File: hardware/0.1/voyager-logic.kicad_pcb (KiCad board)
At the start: 6 copper layers, 0 parts

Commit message: finalise BOM
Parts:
- added C201: 4u7, Capacitor_SMD:C_0402_1005Metric, F.Cu at (120.8, 54.4)
- added C202: 10u, Capacitor_SMD:C_0603_1608Metric, F.Cu at (110.0, 65.5)
- added C203: 470n, Capacitor_SMD:C_0402_1005Metric, F.Cu at (118.0, 56.9)
- added C204: 100n, Capacitor_SMD:C_0402_1005Metric, F.Cu at (116.6, 58.9)
- added C205: 470n, Capacitor_SMD:C_0402_1005Metric, F.Cu at (122.3, 52.4)
- added C206: 470n, Capacitor_SMD:C_0402_1005Metric, F.Cu at (112.6, 52.6)
- added C207: 470n, Capacitor_SMD:C_0402_1005Metric, F.Cu at (124.0, 50.4)
- added C208: 100n, Capacitor_SMD:C_0402_1005Metric, F.Cu at (118.0, 55.0)
- added C301: 100n, Capacitor_SMD:C_0402_1005Metric, F.Cu at (145.7, 64.8)
- added C302: 100n, Capacitor_SMD:C_0402_1005Metric, F.Cu at (150.2, 60.8)
- added C303: 13p, Capacitor_SMD:C_0402_1005Metric, F.Cu at (154.2, 56.3)
- added C304: 13p, Capacitor_SMD:C_0402_1005Metric, F.Cu at (157.1, 54.3)
- added C305: 100n, Capacitor_SMD:C_0402_1005Metric, F.Cu at (157.1, 52.3)
- added C306: 100n, Capacitor_SMD:C_0402_1005Metric, F.Cu at (148.6, 62.8)
- added C401: 100n, Capacitor_SMD:C_0402_1005Metric, F.Cu at (130.6, 54.3)
- added C501: 100n, Capacitor_SMD:C_0402_1005Metric, F.Cu at (178.3, 100.6)
- added C502: 100n, Capacitor_SMD:C_0402_1005Metric, F.Cu at (187.2, 91.7)
- added C701: 10u, Capacitor_SMD:C_0603_1608Metric, F.Cu at (121.8, 130.7)
- added C702: 10u, Capacitor_SMD:C_0603_1608Metric, F.Cu at (125.8, 132.7)
- added C703: 6p8, Capacitor_SMD:C_0402_1005Metric, F.Cu at (131.1, 144.2)
- added C704: 4u7, Capacitor_SMD:C_0402_1005Metric, F.Cu at (145.0, 129.1)
- added C705: 10u, Capacitor_SMD:C_0603_1608Metric, F.Cu at (121.8, 133.2)
- added C706: 100n, Capacitor_SMD:C_0402_1005Metric, F.Cu at (130.6, 140.2)
- added C707: 100n, Capacitor_SMD:C_0402_1005Metric, F.Cu at (135.2, 135.4)
- added C708: 100n, Capacitor_SMD:C_0402_1005Metric, F.Cu at (146.6, 127.1)
- added C709: 100n, Capacitor_SMD:C_0402_1005Metric, F.Cu at (145.0, 131.1)
- added C710: 100n, Capacitor_SMD:C_0402_1005Metric, F.Cu at (139.2, 129.1)
- added C711: 100n, Capacitor_SMD:C_0402_1005Metric, F.Cu at (133.5, 137.4)
- added C712: 10u, Capacitor_SMD:C_0603_1608Metric, F.Cu at (117.2, 141.2)
- added C713: 100n, Capacitor_SMD:C_0402_1005Metric, F.Cu at (136.4, 139.3)
- added C714: 100n, Capacitor_SMD:C_0402_1005Metric, F.Cu at (136.4, 137.4)
- added C715: 100n, Capacitor_SMD:C_0402_1005Metric, F.Cu at (131.1, 142.2)
- added C716: 100n, Capacitor_SMD:C_0402_1005Metric, F.Cu at (142.1, 129.1)
- added C717: 100n, Capacitor_SMD:C_0402_1005Metric, F.Cu at (138.1, 135.0)
- added C718: 4u7, Capacitor_SMD:C_0402_1005Metric, F.Cu at (127.7, 140.2)
- added C719: 100n, Capacitor_SMD:C_0402_1005Metric, F.Cu at (128.3, 142.2)
- added C720: 100n, Capacitor_SMD:C_0402_1005Metric, F.Cu at (140.9, 133.1)
- added C721: 10u, Capacitor_SMD:C_0603_1608Metric, F.Cu at (130.7, 127.4)
- added C722: 10u, Capacitor_SMD:C_0603_1608Metric, F.Cu at (121.3, 138.2)
- added C723: 6p8, Capacitor_SMD:C_0402_1005Metric, F.Cu at (130.7, 138.2)
- added C724: 4u7, Capacitor_SMD:C_0402_1005Metric, F.Cu at (125.4, 143.2)
- added C725: 10u, Capacitor_SMD:C_0603_1608Metric, F.Cu at (117.2, 138.7)
- added C726: 10u, Capacitor_SMD:C_0603_1608Metric, F.Cu at (125.8, 130.1)
- added C727: 100n, Capacitor_SMD:C_0402_1005Metric, F.Cu at (143.7, 127.1)
- added C728: 100n, Capacitor_SMD:C_0402_1005Metric, F.Cu at (142.1, 131.1)
- added C729: 100n, Capacitor_SMD:C_0402_1005Metric, F.Cu at (133.5, 139.4)
- added C730: 10u, Capacitor_SMD:C_0603_1608Metric, F.Cu at (129.8, 129.9)
- added C731: 10u, Capacitor_SMD:C_0603_1608Metric, F.Cu at (121.8, 135.7)
- added C732: 100n, Capacitor_SMD:C_0402_1005Metric, F.Cu at (138.1, 133.1)
- added C733: 100n, Capacitor_SMD:C_0402_1005Metric, F.Cu at (139.2, 131.1)
- added C734: 10u, Capacitor_SMD:C_0603_1608Metric, F.Cu at (126.7, 127.4)
- added C735: 10u, Capacitor_SMD:C_0603_1608Metric, F.Cu at (117.2, 136.2)
- added C736: 6p8, Capacitor_SMD:C_0402_1005Metric, F.Cu at (135.2, 133.4)
- added C737: 4u7, Capacitor_SMD:C_0402_1005Metric, F.Cu at (128.3, 144.2)
- added D201: SMF9.0CA, josh-passives-smt:D_SOD-123FL, F.Cu at (110.1, 62.8)
- added D202: DESD5V0U1BL, josh-passives-smt:D_X1-DFN1006-2, F.Cu at (114.4, 62.8)
- added D203: DESD5V0U1BL, josh-passives-smt:D_X1-DFN1006-2, F.Cu at (111.5, 55.4)
- added D401: LED_RGBA, josh-led:LED_TRI_2020, F.Cu at (110.3, 107.4)
- added D402: LED_RGBA, josh-led:LED_TRI_2020, F.Cu at (110.3, 79.6)
- added D501: DESD5V0U1BL, josh-passives-smt:D_X1-DFN1006-2, F.Cu at (166.4, 88.2)
- added D502: DESD5V0U1BL, josh-passives-smt:D_X1-DFN1006-2, F.Cu at (164.7, 101.5)
- added D503: DESD5V0U1BL, josh-passives-smt:D_X1-DFN1006-2, F.Cu at (174.9, 91.2)
- added D504: DESD5V0U1BL, josh-passives-smt:D_X1-DFN1006-2, F.Cu at (166.4, 97.1)
- added D505: DESD5V0U1BL, josh-passives-smt:D_X1-DFN1006-2, F.Cu at (166.4, 94.2)
- added D506: DESD5V0U1BL, josh-passives-smt:D_X1-DFN1006-2, F.Cu at (179.2, 88.2)
- added D507: DESD5V0U1BL, josh-passives-smt:D_X1-DFN1006-2, F.Cu at (174.9, 88.2)
- added D508: DESD5V0U1BL, josh-passives-smt:D_X1-DFN1006-2, F.Cu at (170.7, 94.2)
- added D509: DESD5V0U1BL, josh-passives-smt:D_X1-DFN1006-2, F.Cu at (170.7, 91.2)
- added D510: DESD5V0U1BL, josh-passives-smt:D_X1-DFN1006-2, F.Cu at (168.9, 100.0)
- added D511: DESD5V0U1BL, josh-passives-smt:D_X1-DFN1006-2, F.Cu at (160.4, 101.5)
- added D512: DESD5V0U1BL, josh-passives-smt:D_X1-DFN1006-2, F.Cu at (170.7, 88.2)
- added D513: DESD5V0U1BL, josh-passives-smt:D_X1-DFN1006-2, F.Cu at (174.9, 94.2)
- added D514: DESD5V0U1BL, josh-passives-smt:D_X1-DFN1006-2, F.Cu at (179.2, 91.2)
- added D515: DESD5V0U1BL, josh-passives-smt:D_X1-DFN1006-2, F.Cu at (170.7, 97.1)
- added D516: DESD5V0U1BL, josh-passives-smt:D_X1-DFN1006-2, F.Cu at (166.4, 91.2)
- added F201: 500mA, josh-passives-smt:Fuse_0603_1608Metric, F.Cu at (115.9, 52.7)
- added FB201: 220R, Resistor_SMD:R_0402_1005Metric, F.Cu at (121.1, 50.4)
- added FB202: 220R, Resistor_SMD:R_0402_1005Metric, F.Cu at (113.7, 59.9)
- added FB701: 220R, Resistor_SMD:R_0402_1005Metric, F.Cu at (122.5, 143.7)
- added FB702: 220R, Resistor_SMD:R_0402_1005Metric, F.Cu at (140.8, 127.1)
- added FB703: 220R, Resistor_SMD:R_0402_1005Metric, F.Cu at (136.3, 130.4)
- added FB704: 220R, Resistor_SMD:R_0402_1005Metric, F.Cu at (127.8, 138.3)
- added H201: M2, MountingHole:MountingHole_2.2mm_M2_ISO7380_Pad, F.Cu at (110.0, 71.5)
- added H202: M2, MountingHole:MountingHole_2.2mm_M2_ISO7380_Pad, F.Cu at (155.0, 71.5)
- added H203: M2, MountingHole:MountingHole_2.2mm_M2_ISO7380_Pad, F.Cu at (110.0, 116.5)
- added H204: M2, MountingHole:MountingHole_2.2mm_M2_ISO7380_Pad, F.Cu at (155.0, 116.5)
- added J201: USB_C_Receptacle, josh-connectors:USB_C_Receptacle_Amphenol_10137062-00021LF, F.Cu at (110.3, 94.0)
- added J401: JTAG, Connector:Tag-Connect_TC2030-IDC-NL_2x03_P1.27mm_Vertical, F.Cu at (178.3, 58.6)
- added J402: JTAG, Connector:Tag-Connect_TC2030-IDC-NL_2x03_P1.27mm_Vertical, F.Cu at (167.3, 60.2)
- added J501: Probe, josh-connectors:PinSocket_2x16_P1.27mm_Horizontal, F.Cu at (151.4, 103.5)
- added L701: 2u2, Inductor_SMD:L_0805_2012Metric, F.Cu at (117.5, 133.6)
- added L702: 2u2, Inductor_SMD:L_0805_2012Metric, F.Cu at (117.5, 130.8)
- added L703: 2u2, Inductor_SMD:L_0805_2012Metric, F.Cu at (122.4, 127.5)
- added R201: 909K, Resistor_SMD:R_0402_1005Metric, F.Cu at (113.7, 57.9)
- added R202: 10K, Resistor_SMD:R_0402_1005Metric, F.Cu at (116.5, 65.4)
- added R203: 200K, Resistor_SMD:R_0402_1005Metric, F.Cu at (121.1, 48.4)
- added R204: 200K, Resistor_SMD:R_0402_1005Metric, F.Cu at (109.7, 52.6)
- added R205: 200K, Resistor_SMD:R_0402_1005Metric, F.Cu at (119.4, 52.5)
- added R206: 0R, Resistor_SMD:R_0402_1005Metric, F.Cu at (115.1, 55.0)
- added R207: 0R, Resistor_SMD:R_0402_1005Metric, F.Cu at (124.0, 48.4)
- added R301: 10K, Resistor_SMD:R_0402_1005Metric, F.Cu at (138.5, 65.4)
- added R302: 200R, Resistor_SMD:R_0402_1005Metric, F.Cu at (145.7, 62.8)
- added R303: 6K04, Resistor_SMD:R_0402_1005Metric, F.Cu at (141.4, 65.4)
- added R304: 2K2, Resistor_SMD:R_0402_1005Metric, F.Cu at (154.2, 54.3)
- added R305: 2K2, Resistor_SMD:R_0402_1005Metric, F.Cu at (150.2, 58.8)
- added R306: 10K, Resistor_SMD:R_0402_1005Metric, F.Cu at (135.6, 65.4)
- added R307: DNP, Resistor_SMD:R_0402_1005Metric, F.Cu at (154.2, 52.3)
- added R308: 10K, Resistor_SMD:R_0402_1005Metric, F.Cu at (132.7, 65.4)
- added R401: 1K, Resistor_SMD:R_0402_1005Metric, F.Cu at (127.7, 57.6)
- added R402: 10K, Resistor_SMD:R_0402_1005Metric, F.Cu at (132.7, 52.3)
- added R403: 1K, Resistor_SMD:R_0402_1005Metric, F.Cu at (127.7, 55.6)
- added R404: 1K, Resistor_SMD:R_0402_1005Metric, F.Cu at (129.8, 52.3)
- added R405: 1K, Resistor_SMD:R_0402_1005Metric, F.Cu at (124.8, 55.6)
- added R406: 1K, Resistor_SMD:R_0402_1005Metric, F.Cu at (120.9, 58.9)
- added R407: 1K, Resistor_SMD:R_0402_1005Metric, F.Cu at (124.8, 57.6)
- added R408: DNP, Resistor_SMD:R_0402_1005Metric, F.Cu at (140.4, 135.3)
- added R409: 0R0, Resistor_SMD:R_0402_1005Metric, F.Cu at (143.3, 135.3)
- added R501: 0R, Resistor_SMD:R_0402_1005Metric, F.Cu at (178.5, 93.7)
- added R502: 0R, Resistor_SMD:R_0402_1005Metric, F.Cu at (175.4, 100.6)
- added R503: 909K, Resistor_SMD:R_0402_1005Metric, F.Cu at (184.3, 93.7)
- added R504: 909K, Resistor_SMD:R_0402_1005Metric, F.Cu at (172.5, 99.6)
- added R505: 909K, Resistor_SMD:R_0402_1005Metric, F.Cu at (188.6, 89.8)
- added R506: 909K, Resistor_SMD:R_0402_1005Metric, F.Cu at (168.2, 102.5)
- added R507: 909K, Resistor_SMD:R_0402_1005Metric, F.Cu at (188.6, 87.8)
- added R508: 909K, Resistor_SMD:R_0402_1005Metric, F.Cu at (185.7, 87.8)
- added R509: 909K, Resistor_SMD:R_0402_1005Metric, F.Cu at (182.8, 87.8)
- added R510: 909K, Resistor_SMD:R_0402_1005Metric, F.Cu at (174.3, 96.6)
- added R511: 0R, Resistor_SMD:R_0402_1005Metric, F.Cu at (177.2, 96.6)
- added R512: 909K, Resistor_SMD:R_0402_1005Metric, F.Cu at (174.1, 102.6)
- added R513: 909K, Resistor_SMD:R_0402_1005Metric, F.Cu at (178.3, 98.6)
- added R514: 909K, Resistor_SMD:R_0402_1005Metric, F.Cu at (171.1, 102.5)
- added R515: 909K, Resistor_SMD:R_0402_1005Metric, F.Cu at (184.3, 91.8)
- added R516: 0R, Resistor_SMD:R_0402_1005Metric, F.Cu at (182.8, 89.8)
- added R517: 909K, Resistor_SMD:R_0402_1005Metric, F.Cu at (180.1, 95.7)
- added R518: 909K, Resistor_SMD:R_0402_1005Metric, F.Cu at (175.4, 98.6)
- added R519: 909K, Resistor_SMD:R_0402_1005Metric, F.Cu at (181.4, 93.7)
- added R520: 909K, Resistor_SMD:R_0402_1005Metric, F.Cu at (185.7, 89.8)
- added R701: 120K, Resistor_SMD:R_0402_1005Metric, F.Cu at (124.5, 141.2)
- added R702: 26K7, Resistor_SMD:R_0402_1005Metric, F.Cu at (119.6, 143.7)
- added R703: 120K, Resistor_SMD:R_0402_1005Metric, F.Cu at (132.3, 133.4)
- added R704: 120K, Resistor_SMD:R_0402_1005Metric, F.Cu at (132.1, 135.4)
- added R705: 120K, Resistor_SMD:R_0402_1005Metric, F.Cu at (137.9, 127.1)
- added R706: 60K4, Resistor_SMD:R_0402_1005Metric, F.Cu at (116.7, 143.5)
- added SW401: KMR2, josh-buttons-switches:SW_Push_KMR2, F.Cu at (140.6, 57.1)
- added TP201: TP, josh-test-point:TestPoint_SMDPad_D0.5mm_NO_SILK, F.Cu at (118.0, 62.8)
- added TP202: TP, josh-test-point:TestPoint_SMDPad_D0.5mm_NO_SILK, F.Cu at (113.5, 65.8)
- added TP701: TP, josh-test-point:TestPoint_SMDPad_D0.5mm_NO_SILK, F.Cu at (133.3, 130.9)
- added TP702: TP, josh-test-point:TestPoint_SMDPad_D0.5mm_NO_SILK, F.Cu at (129.1, 135.7)
- added TP703: TP, josh-test-point:S1751-46_smdTestPoint, F.Cu at (117.7, 127.8)
- added TP704: TP, josh-test-point:TestPoint_SMDPad_D0.5mm_NO_SILK, F.Cu at (129.3, 132.7)
- added TP705: TP, josh-test-point:TestPoint_SMDPad_D0.5mm_NO_SILK, F.Cu at (124.8, 138.7)
- added U201: TPD4EUSB30, Package_SON:USON-10_2.5x1.0mm_P0.5mm, F.Cu at (122.5, 93.5)
- added U202: HD3SS3220, josh-dfn-qfn:Texas_RNH0030A_WQFN-30_2.5x4.5mm_P0.4mm, F.Cu at (128.3, 93.6)
- added U203: TPD4EUSB30, Package_SON:USON-10_2.5x1.0mm_P0.5mm, F.Cu at (120.1, 95.4)
- added U204: TPD4EUSB30, Package_SON:USON-10_2.5x1.0mm_P0.5mm, F.Cu at (120.1, 91.6)
- added U301: CYUSB3014-BZXx, josh-bga:BGA-121_10x10mm_Layout11x11_P0.8mm, F.Cu at (137.7, 94.0)
- added U302: M24M02, Package_SO:SOIC-8_3.9x4.9mm_P1.27mm, F.Cu at (148.5, 54.5)
- added U501: SN74LVC245A, josh-dfn-qfn:Texas_RGY0020A_VQFN-20_2.5x4.5mm_P0.5mm, F.Cu at (141.2, 108.2)
- added U502: SN74LVC245A, josh-dfn-qfn:Texas_RGY0020A_VQFN-20_2.5x4.5mm_P0.5mm, F.Cu at (140.8, 79.8)
- added U701: TLV62569DRLR, Package_TO_SOT_SMD:SOT-563, F.Cu at (121.1, 141.1)
- added U703: TLV62569DRLR, Package_TO_SOT_SMD:SOT-563, F.Cu at (125.7, 135.5)
- added U704: TLV62569DRLR, Package_TO_SOT_SMD:SOT-563, F.Cu at (134.6, 127.8)
- added Y301: 19.2MHz, josh-oscillators:Crystal_SMD_2520-4Pin_2.5x2.0mm, F.Cu at (146.5, 59.8)
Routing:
- added copper zone on In2.Cu, net +3V3
- added copper zone on In1.Cu, net GND
- added copper zone on In3.Cu, net GND
- added copper zone on In4.Cu, net GND
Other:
- board outline added: 50 x 50 mm
- board text added: "Layer Stack: 1: Impedance controlled signal 2: GND 3: 3V3 / VIO 4: Signal 5: GND 6: Impedance controlled signal"

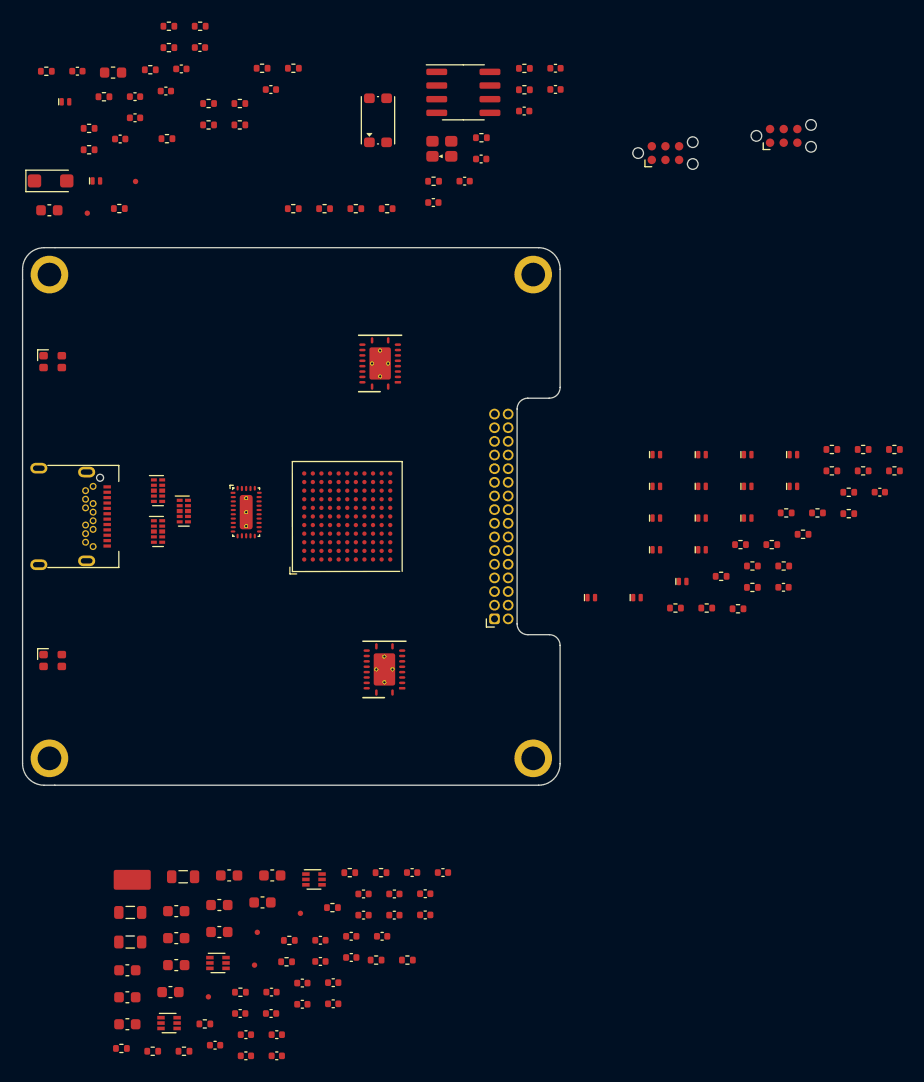
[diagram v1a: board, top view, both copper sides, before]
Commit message: all components fit inside outline
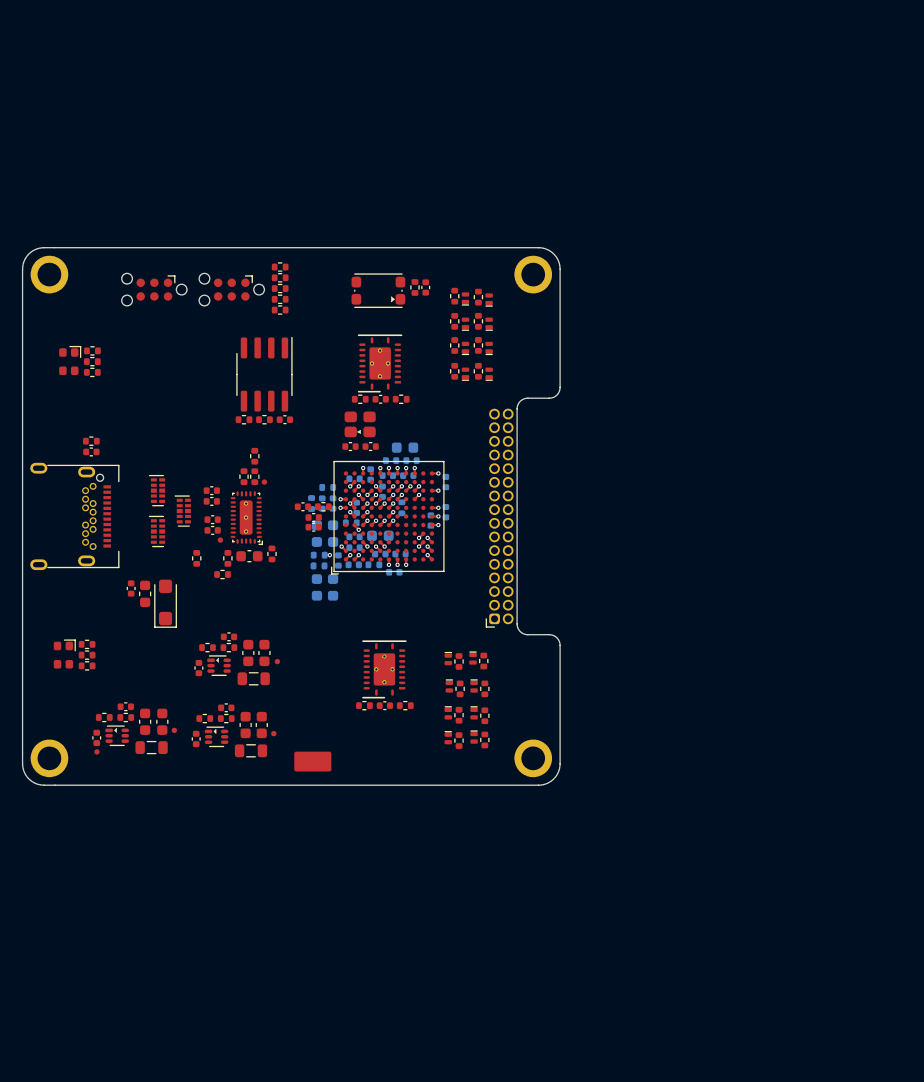
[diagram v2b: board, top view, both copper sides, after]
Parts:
- removed D202, D203: DESD5V0U1BL, josh-passives-smt:D_X1-DFN1006-2
- C305, C705, C706, C707, C708, C709, C710, C711, C712, C713, C714, C715, C716, C717, C718, C719, C720, C725, C726, C727, C728, C729, C730, C731, C732, C733, FB701, FB702, FB703, FB704, R301, R302, R303: moved to B.Cu
- U701, U703, U704: footprint Package_TO_SOT_SMD:SOT-563 -> josh-soic-sot-etc:SOT-563
- moved R408 65.1 mm to (131.5, 70.8)
- moved R409 64.6 mm to (131.5, 71.8)
- moved J401 60.3 mm to (119.8, 72.9), turned to 180 degrees
- moved R404 57.9 mm to (113.5, 107.9)
- moved R403 53.2 mm to (113.5, 106.9)
- moved FB701 52.3 mm to (134.4, 92.8), turned to 90 degrees
- moved C712 51.2 mm to (140.8, 95.8)
- moved R207 51.0 mm to (126.1, 99.4)
- moved R401 50.4 mm to (113.5, 105.9)
- moved C705 50.3 mm to (143.1, 87.6), turned to 180 degrees
- moved C719 50.1 mm to (136.4, 92.8), turned to 90 degrees
- moved C715 49.9 mm to (145.5, 94.4), turned to 90 degrees
- moved R203 49.8 mm to (126.6, 97.9), turned to 90 degrees
- moved C729 49.7 mm to (139.9, 90.1), turned to -90 degrees
- moved C706 49.6 mm to (141.0, 91.7), turned to -90 degrees
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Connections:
- U201 pad 4: unconnected-(U201-Pad4) -> /USB C Connector/CC1
- U201 pad 5: unconnected-(U201-Pad5) -> /USB C Connector/CC2
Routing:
- net GND: track 0.00 -> 8.92 mm, vias 0 -> 15
- net +1V2: track 0.00 -> 4.88 mm, vias 0 -> 9
- net VIO: track 0.00 -> 2.17 mm, vias 0 -> 4
- net +3V3: track 0.00 -> 1.07 mm, vias 0 -> 2
- net /Power/U3TX_VDDQ: track 0.00 -> 0.61 mm, vias 0 -> 1
- net Net-(R303-Pad1): track 0.00 -> 0.57 mm, vias 0 -> 1
- net Net-(C304-Pad1): track 0.00 -> 0.57 mm, vias 0 -> 1
- net Net-(C303-Pad1): track 0.00 -> 0.57 mm, vias 0 -> 1
- net /Power/U3RX_VDDQ: track 0.00 -> 0.57 mm, vias 0 -> 1
- net /Power/CVDDQ: track 0.00 -> 0.57 mm, vias 0 -> 1
- net /FX3 Logic Inputs/CH_15: track 0.00 -> 0.57 mm, vias 0 -> 1
- net /FX3 Logic Inputs/CH_14: track 0.00 -> 0.57 mm, vias 0 -> 1
- net /Debug/JTAG_TDI: track 0.00 -> 0.57 mm, vias 0 -> 1
- net /FX3 Logic Inputs/CH_9: track 0.00 -> 0.57 mm, vias 0 -> 1
- net /FX3 Logic Inputs/CH_7: track 0.00 -> 0.57 mm, vias 0 -> 1
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
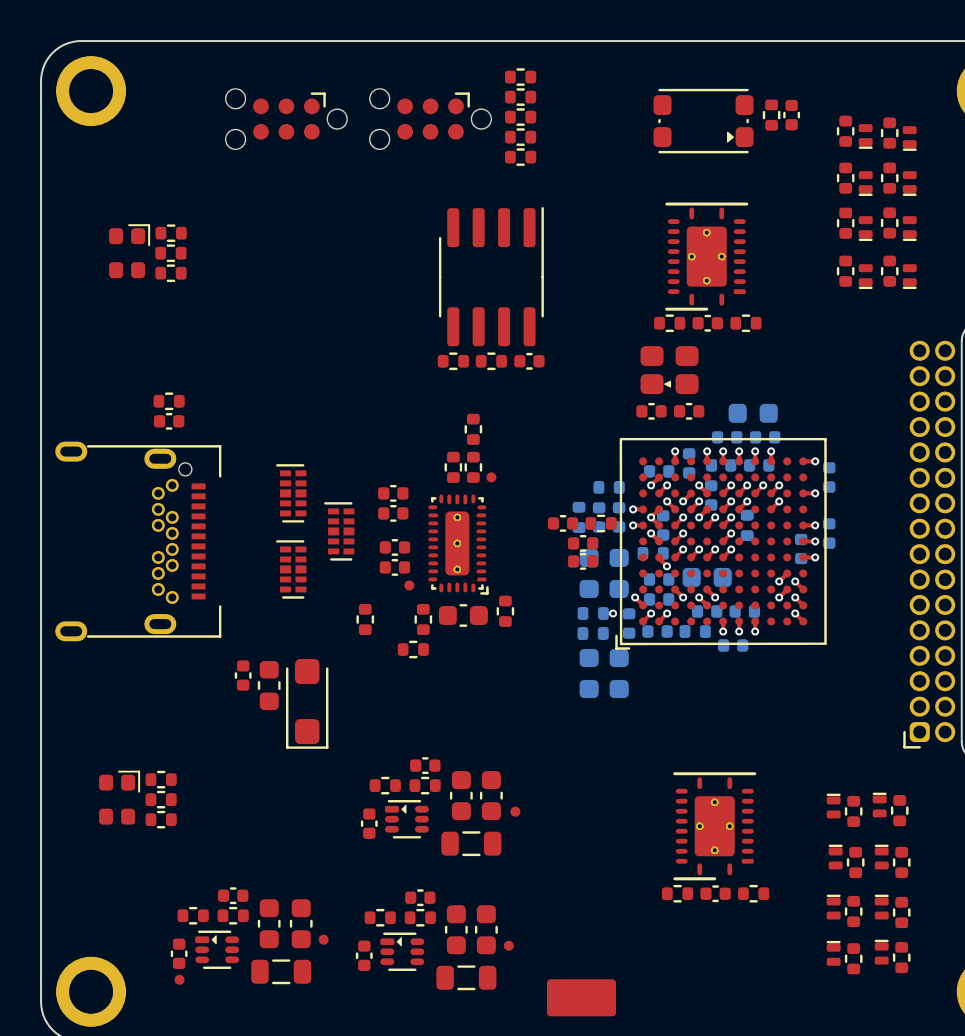
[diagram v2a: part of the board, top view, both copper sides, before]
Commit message: break out bga
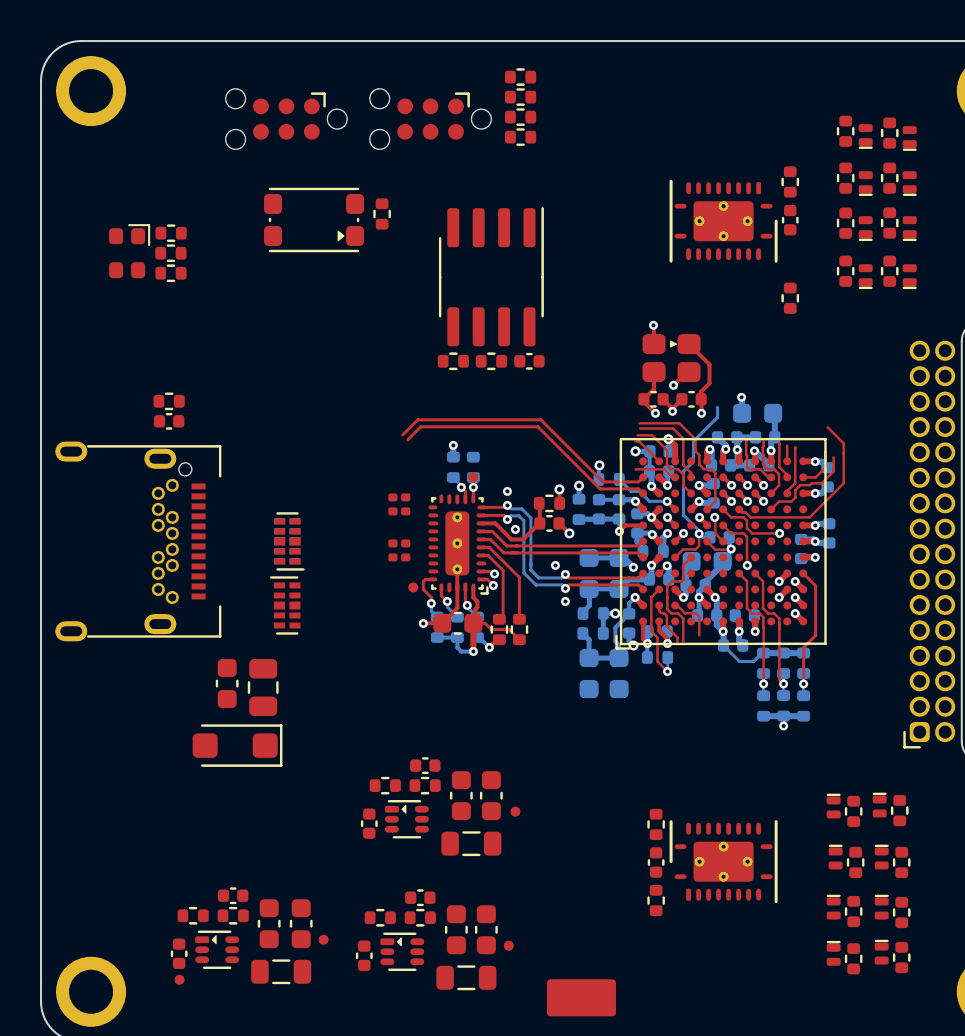
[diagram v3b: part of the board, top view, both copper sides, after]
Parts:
- removed C301, C302: 100n, Capacitor_SMD:C_0402_1005Metric
- removed D401: LED_RGBA, josh-led:LED_TRI_2020
- removed R301, R308: 10K, Resistor_SMD:R_0402_1005Metric
- removed R401, R403, R404: 1K, Resistor_SMD:R_0402_1005Metric
- added R601: DNP, Resistor_SMD:R_0402_1005Metric, B.Cu at (145.6, 100.1)
- added R602: 10K, Resistor_SMD:R_0402_1005Metric, B.Cu at (144.6, 100.1)
- added R603: 10K, Resistor_SMD:R_0402_1005Metric, B.Cu at (143.6, 100.1)
- added R604: DNP, Resistor_SMD:R_0402_1005Metric, B.Cu at (145.6, 102.2)
- added R605: DNP, Resistor_SMD:R_0402_1005Metric, B.Cu at (144.6, 102.2)
- added R606: DNP, Resistor_SMD:R_0402_1005Metric, B.Cu at (143.6, 102.2)
- C201: value 4u7 -> 10u; footprint Capacitor_SMD:C_0402_1005Metric -> Capacitor_SMD:C_0603_1608Metric
- C203, C205, C206, C207: value 470n -> 100n; footprint Capacitor_SMD:C_0402_1005Metric -> Capacitor_SMD:C_0201_0603Metric
- C401, R203, R204, R205, R206, R207, U204: moved to B.Cu
- F201: footprint josh-passives-smt:Fuse_0603_1608Metric -> josh-passives-smt:Fuse_0805_2012Metric
- moved C401 21.4 mm to (141.4, 93.8), turned to 0 degrees
- moved R402 20.1 mm to (124.5, 77.6)
- moved SW401 20.1 mm to (121.1, 77.9)
- moved R201 10.3 mm to (131.4, 98.4)
- moved R511 7.40 mm to (144.9, 76.0), turned to 90 degrees
- moved C502 6.60 mm to (144.9, 78.0), turned to -90 degrees
- moved R516 6.15 mm to (144.9, 81.8), turned to -90 degrees
- moved R501 4.88 mm to (138.2, 111.9), turned to -90 degrees
- moved U201 4.58 mm to (119.8, 97.2)
- moved D201 4.22 mm to (117.2, 104.2), turned to 180 degrees
- moved R502 3.62 mm to (138.2, 108.1), turned to 90 degrees
- moved R204 3.62 mm to (127.3, 98.3)
- moved R207 3.39 mm to (129.3, 98.3), turned to 90 degrees
- moved C501 3.35 mm to (138.2, 110.0), turned to 90 degrees
- moved FB201 2.77 mm to (132.9, 92.1)
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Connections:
- net Net-(C203-Pad2) renamed /USB C Connector/TX2-
- net Net-(C205-Pad2) renamed /USB C Connector/TX2+
- net Net-(C206-Pad1) renamed /USB C Connector/TX1N
- net Net-(C206-Pad2) renamed /USB C Connector/TX1-
- net Net-(C207-Pad1) renamed /USB C Connector/TX1P
- net Net-(C207-Pad2) renamed /USB C Connector/TX1+
- C203 pad 1: Net-(C203-Pad1) -> /USB C Connector/TX2N
- C205 pad 1: Net-(C205-Pad1) -> /USB C Connector/TX2P
- J201 pad A2: Net-(J201-PadA2) -> /USB C Connector/RX2P
- J201 pad A3: Net-(J201-PadA3) -> /USB C Connector/RX2N
- J201 pad B10: Net-(C203-Pad1) -> /USB C Connector/TX2N
- J201 pad B11: Net-(C205-Pad1) -> /USB C Connector/TX2P
- J201 pad B2: Net-(J201-PadB2) -> /USB C Connector/RX1P
- J201 pad B3: Net-(J201-PadB3) -> /USB C Connector/RX1N
- U202 pad 10: /FX3 USB and Misc/USB3_RX_N -> /FX3 USB and Misc/USB3_RX_P
- U202 pad 14: Net-(J201-PadB3) -> /USB C Connector/RX1N
- U202 pad 15: Net-(J201-PadB2) -> /USB C Connector/RX1P
- U202 pad 18: Net-(J201-PadA3) -> /USB C Connector/RX2N
- U202 pad 19: Net-(J201-PadA2) -> /USB C Connector/RX2P
- U202 pad 9: /FX3 USB and Misc/USB3_RX_P -> /FX3 USB and Misc/USB3_RX_N
- U203 pad 4: Net-(J201-PadB2) -> /USB C Connector/RX2N
- U203 pad 5: Net-(J201-PadB3) -> /USB C Connector/RX2P
- U204 pad 1: Net-(C205-Pad1) -> /USB C Connector/RX1P
- U204 pad 2: Net-(C203-Pad1) -> /USB C Connector/RX1N
- U204 pad 4: Net-(J201-PadA2) -> /USB C Connector/TX2N
- U204 pad 5: Net-(J201-PadA3) -> /USB C Connector/TX2P
- U301 pad A5: Net-(C301-Pad2) -> /FX3 USB and Misc/USB3_TX_P
- U301 pad A6: Net-(C302-Pad2) -> /FX3 USB and Misc/USB3_TX_N
- U301 pad B2: Net-(R301-Pad1) -> GND
- U301 pad B4: Net-(R301-Pad1) -> GND
- U301 pad E1: /Debug/LED_G -> unconnected-(U301-PadE1)
- U301 pad E5: /Debug/LED_B -> unconnected-(U301-PadE5)
- U301 pad E6: Net-(R301-Pad1) -> GND
- U301 pad F5: /Debug/LED_R -> unconnected-(U301-PadF5)
- U301 pad G4: unconnected-(U301-PadG4) -> /FX3 Logic Inputs/PMODE0
- U301 pad H4: unconnected-(U301-PadH4) -> /FX3 Logic Inputs/PMODE1
- U301 pad L4: unconnected-(U301-PadL4) -> /FX3 Logic Inputs/PMODE2
- Y301 pad 1: Net-(C304-Pad1) -> Net-(C303-Pad1)
- Y301 pad 3: Net-(C303-Pad1) -> Net-(C304-Pad1)
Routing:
- net GND: track 8.92 -> 50.9 mm, vias 15 -> 34
- net VIO: track 2.17 -> 33.8 mm
- net /FX3 Logic Inputs/CH_3: track 0.00 -> 14.4 mm, vias 0 -> 1
- net /FX3 USB and Misc/USB2_D-: track 0.00 -> 13.7 mm
- net /FX3 USB and Misc/USB2_D+: track 0.00 -> 13.4 mm
- net /FX3 Logic Inputs/CH_6: track 0.00 -> 12.3 mm, vias 0 -> 1
- net /FX3 Logic Inputs/CH_0: track 0.00 -> 12.1 mm, vias 0 -> 1
- net /FX3 Logic Inputs/CH_5: track 0.57 -> 12.6 mm
- net /FX3 USB and Misc/USB3_RX_P: track 0.00 -> 11.5 mm, vias 0 -> 2
- net /FX3 USB and Misc/USB3_RX_N: track 0.00 -> 11.4 mm, vias 0 -> 2
- net +3V3: track 1.07 -> 11.9 mm, vias 2 -> 4
- net /FX3 Logic Inputs/CH_4: track 0.57 -> 11.2 mm
- net +1V2: track 4.88 -> 15.5 mm, vias 9 -> 10
- net Net-(C303-Pad1): track 0.57 -> 11.1 mm, vias 1 -> 2
- net /FX3 Logic Inputs/CH_1: track 0.57 -> 11.0 mm
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- added copper zone on In2.Cu, net +1V2

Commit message: more io routing
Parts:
- moved R516 2.05 mm to (145.0, 79.8), turned to 90 degrees
- moved C502 0.09 mm to (145.0, 77.9)
- moved R511 0.08 mm to (145.0, 76.0)
- turned R502 to -90 degrees
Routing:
- net /FX3 Logic Inputs/CH_12: track 1.87 -> 17.2 mm, vias 0 -> 2
- net /FX3 Logic Inputs/CH_13: track 2.47 -> 17.8 mm, vias 0 -> 2
- net /FX3 Logic Inputs/CH_9: track 3.42 -> 18.7 mm
- net /FX3 Logic Inputs/CH_11: track 2.13 -> 16.1 mm, vias 0 -> 2
- net /FX3 Logic Inputs/CH_8: track 2.85 -> 16.5 mm, vias 0 -> 2
- net /FX3 Logic Inputs/CH_14: track 4.83 -> 17.8 mm, vias 0 -> 2
- net VIO: track 33.8 -> 46.7 mm, vias 4 -> 6
- net /FX3 Logic Inputs/CH_15: track 9.22 -> 21.7 mm, vias 0 -> 2
- net /FX3 Logic Inputs/CH_4: track 11.2 -> 23.4 mm, vias 1 -> 2
- net /FX3 Logic Inputs/CH_10: track 0.78 -> 11.4 mm
- net /FX3 Logic Inputs/CH_7: track 10.4 -> 18.4 mm, vias 1 -> 2
- net /FX3 Logic Inputs/CH_0: track 12.1 -> 19.8 mm, vias 1 -> 2
- net /FX3 Logic Inputs/CH_1: track 11.0 -> 18.7 mm, vias 1 -> 2
- net /FX3 Logic Inputs/CH_6: track 12.3 -> 19.8 mm, vias 1 -> 2
- net /FX3 Logic Inputs/CH_2: track 8.96 -> 15.8 mm, vias 1 -> 2
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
